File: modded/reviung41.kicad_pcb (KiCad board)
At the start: 2 copper layers, 225.1 x 119 mm, 85 parts, among them SW10 SW_PUSH, SW11 SW_PUSH, SW12 SW_PUSH, SW14 SW_PUSH, SW15 SW_PUSH, SW16 SW_PUSH, SW17 SW_PUSH, SW18 SW_PUSH, SW19 SW_PUSH, SW2 SW_PUSH, SW20 SW_PUSH, SW21 SW_PUSH, SW22 SW_PUSH, SW23 SW_PUSH, SW25 SW_PUSH, SW26 SW_PUSH, SW27 SW_PUSH, SW28 SW_PUSH, SW29 SW_PUSH, SW3 SW_PUSH, SW31 SW_PUSH, SW32 SW_PUSH, SW33 SW_PUSH, SW34 SW_PUSH, SW35 SW_PUSH, SW37 SW_PUSH, SW38 SW_PUSH, SW39 SW_PUSH, SW4 SW_PUSH, SW40 SW_PUSH, SW41 SW_PUSH, SW42 SW_PUSH, SW5 SW_PUSH, SW6 SW_PUSH, SW8 SW_PUSH, SW9 SW_PUSH, U1 ProMicro

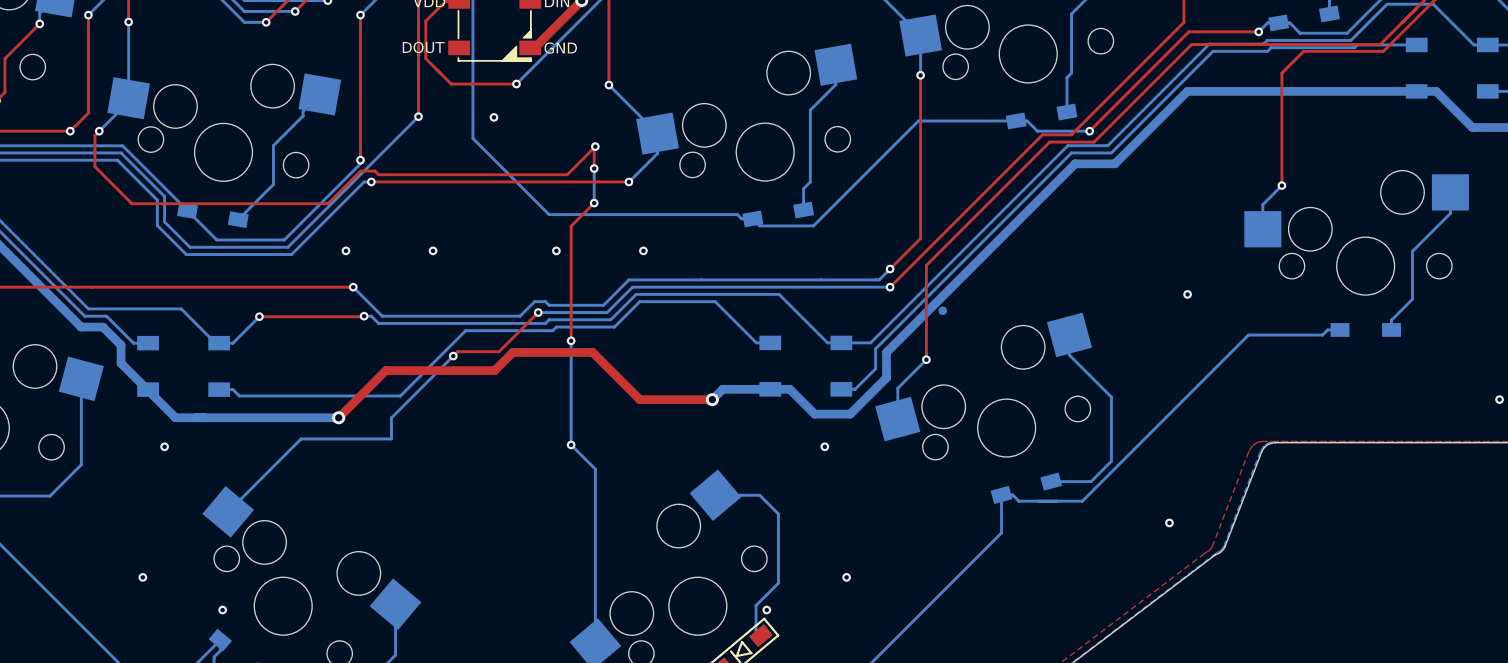
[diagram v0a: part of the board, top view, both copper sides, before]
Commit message: Moved LEDs closer to bottom edge now that pcb dimensions extended
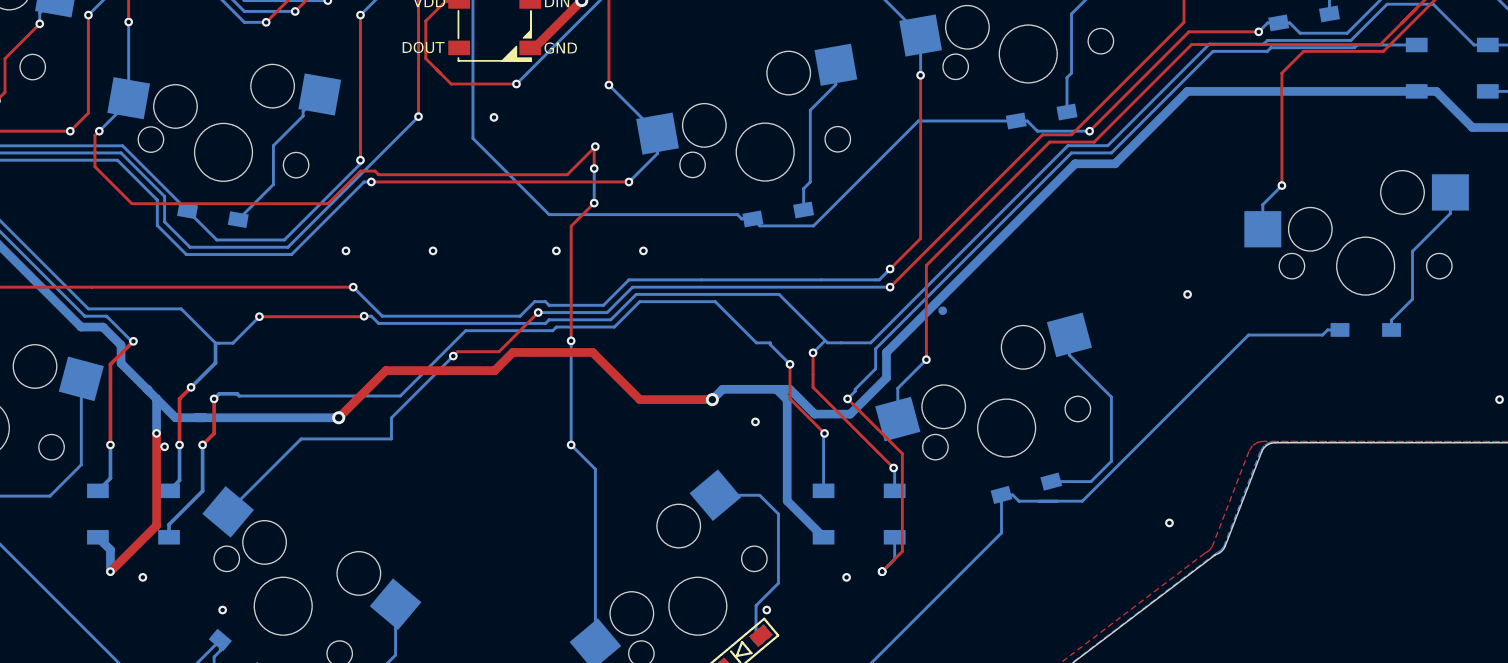
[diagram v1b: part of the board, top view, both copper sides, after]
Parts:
- moved L6 10.8 mm to (169.9, 147.6)
- moved L5 10.7 mm to (119.9, 147.6)
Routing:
- net GND: track 625.5 -> 653.0 mm, vias 43 -> 45
- net VCC: track 546.3 -> 570.7 mm, vias 16 -> 20
- net Net-(L5-Pad2): track 42.0 -> 65.0 mm, vias 0 -> 4
- net Net-(L6-Pad2): track 50.3 -> 67.0 mm, vias 0 -> 3
- net Net-(L4-Pad2): track 46.8 -> 57.3 mm, vias 0 -> 2
